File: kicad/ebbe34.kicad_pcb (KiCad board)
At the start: 2 copper layers, 250.3 x 111.4 mm, 93 parts, among them SW1 SW_SPDT, U2 nice_nano

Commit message: redo outline
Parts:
- removed the ? at (271.0, 59.9)
- removed the ? at (41.2, 107.2)
- removed the ? at (287.9, 107.3)
- removed the ? at (213.3, 63.0)
- removed the REF** at (270.9, 59.9)
- removed the REF** at (287.9, 107.3)
- removed the REF** at (213.3, 63.0)
- removed the REF** at (198.9, 130.3)
- removed the REF** at (164.6, 158.0)
- removed the REF** at (96.3, 112.7)
- removed the REF** at (130.3, 130.3)
- removed the REF** at (58.2, 59.9)
- removed the REF** at (41.2, 107.2)
- removed the REF** at (115.8, 63.0)
- added ?: , , F.Cu at (247.4, 109.5)
- added ?: , , F.Cu at (86.6, 122.0)
- added ?: , , F.Cu at (140.6, 91.9)
- added ?: , , F.Cu at (155.9, 91.9)
- added ?: , , F.Cu at (48.8, 109.5)
- added REF**: Standoff_M2x6mm, ScottoKeebs_Scotto:Standoff_M2x6mm, F.Cu at (140.6, 91.9)
- added REF**: Standoff_M2x6mm, ScottoKeebs_Scotto:Standoff_M2x6mm, F.Cu at (247.4, 109.5)
- added REF**: Standoff_M2x6mm, ScottoKeebs_Scotto:Standoff_M2x6mm, F.Cu at (50.0, 60.9)
- added REF**: Standoff_M2x6mm, ScottoKeebs_Scotto:Standoff_M2x6mm, F.Cu at (101.9, 64.8)
- added REF**: Standoff_M2x6mm, ScottoKeebs_Scotto:Standoff_M2x6mm, F.Cu at (155.9, 91.9)
- added REF**: Standoff_M2x6mm, ScottoKeebs_Scotto:Standoff_M2x6mm, F.Cu at (194.4, 64.8)
- added REF**: Standoff_M2x6mm, ScottoKeebs_Scotto:Standoff_M2x6mm, F.Cu at (86.6, 122.0)
- added REF**: Standoff_M2x6mm, ScottoKeebs_Scotto:Standoff_M2x6mm, F.Cu at (48.8, 109.5)
- added REF**: Standoff_M2x6mm, ScottoKeebs_Scotto:Standoff_M2x6mm, F.Cu at (246.3, 60.9)
- moved SW1 28.6 mm to (148.4, 86.6), turned to 180 degrees
- moved ? 24.8 mm to (209.7, 122.0)
- moved REF** 24.8 mm to (209.7, 122.0)
- moved REF** 17.3 mm to (111.5, 154.1)
- moved REF** 16.7 mm to (148.4, 91.8)
- moved Bat-1 16.6 mm to (142.7, 96.7)
- moved Display1 16.5 mm to (148.1, 113.7)
- moved D19 16.5 mm to (241.6, 82.5)
- moved D1 16.5 mm to (55.2, 78.4)
- moved D10 16.5 mm to (257.1, 72.4)
- moved D11 16.5 mm to (49.4, 94.3)
- moved D12 16.5 mm to (70.7, 88.5)
- moved D13 16.5 mm to (89.0, 90.7)
- moved D16 16.5 mm to (190.9, 101.0)
- moved D17 16.5 mm to (207.3, 93.4)
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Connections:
- net NVCS renamed CS
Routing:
- net RAW: track 29.0 -> 21.5 mm
- net Bat+: track 14.7 -> 9.67 mm
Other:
- board size 250.3 x 111.4 mm -> 249.3 x 113.4 mm

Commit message: move screws
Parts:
- removed the ? at (86.6, 122.0)
- removed the ? at (209.7, 122.0)
- removed the REF** at (209.7, 122.0)
- removed the REF** at (111.5, 154.1)
- removed the REF** at (86.6, 122.0)
- removed the REF** at (184.8, 154.1)
- added ?: , , F.Cu at (138.3, 154.5)
- added ?: , , B.Cu at (158.0, 154.5)
- added REF**: Standoff_M2x6mm, ScottoKeebs_Scotto:Standoff_M2x6mm, F.Cu at (138.3, 154.5)
- added REF**: Standoff_M2x6mm, ScottoKeebs_Scotto:Standoff_M2x6mm, F.Cu at (95.2, 132.7)
- added REF**: Standoff_M2x6mm, ScottoKeebs_Scotto:Standoff_M2x6mm, F.Cu at (158.0, 154.5)
- added REF**: Standoff_M2x6mm, ScottoKeebs_Scotto:Standoff_M2x6mm, F.Cu at (201.1, 132.7)

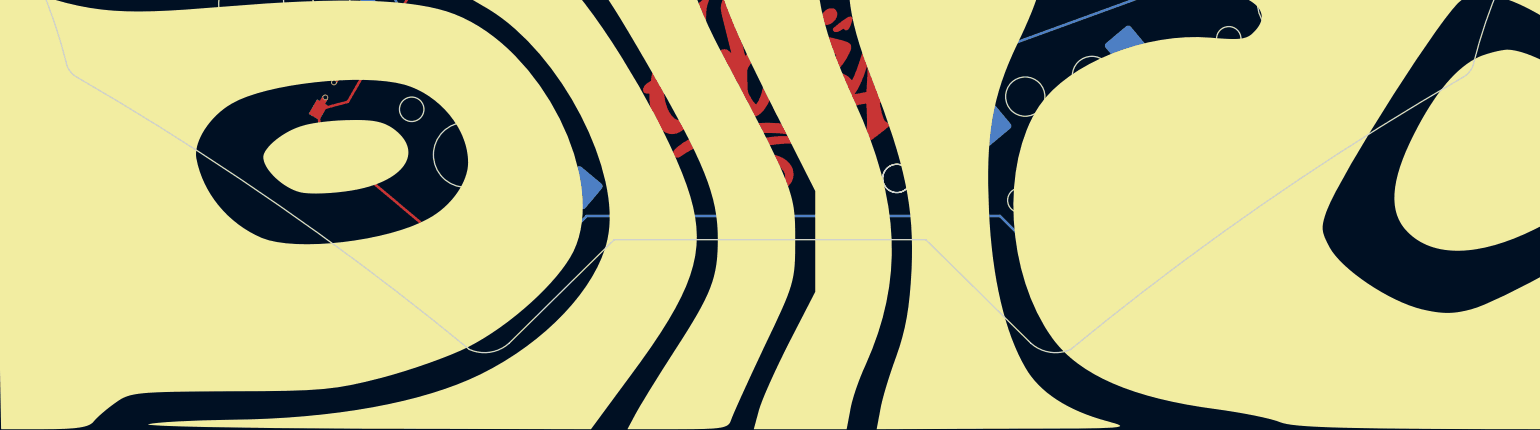
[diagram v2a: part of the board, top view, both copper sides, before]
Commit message: restore bottom curvature
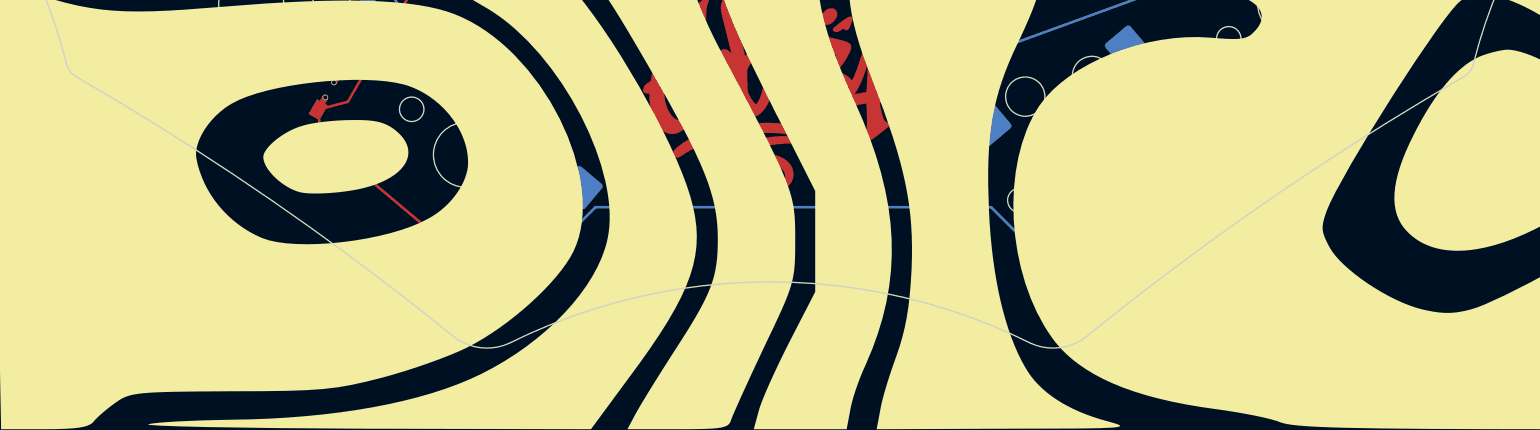
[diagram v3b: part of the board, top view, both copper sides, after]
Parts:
- removed the ? at (138.3, 154.5)
- removed the ? at (158.0, 154.5)
- removed the REF** at (138.3, 154.5)
- removed the REF** at (158.0, 154.5)
- added REF**: Standoff_M2x6mm, ScottoKeebs_Scotto:Standoff_M2x6mm, F.Cu at (148.2, 159.3)
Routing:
- net row 4: track 140.9 -> 141.5 mm
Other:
- board size 249.3 x 113.4 mm -> 249.3 x 113.1 mm
